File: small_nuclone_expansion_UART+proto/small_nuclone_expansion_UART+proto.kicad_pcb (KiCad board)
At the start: 2 copper layers, 50 x 50 mm, 87 parts, among them J1 USB-C_PD_USB, J2 Conn_01x16, J3 nuclone_small_left, J4 nuclone_small_right, J5 127, J6 127, J7 127, J8 127, U1 TPESD0504C6, U2 CH340B

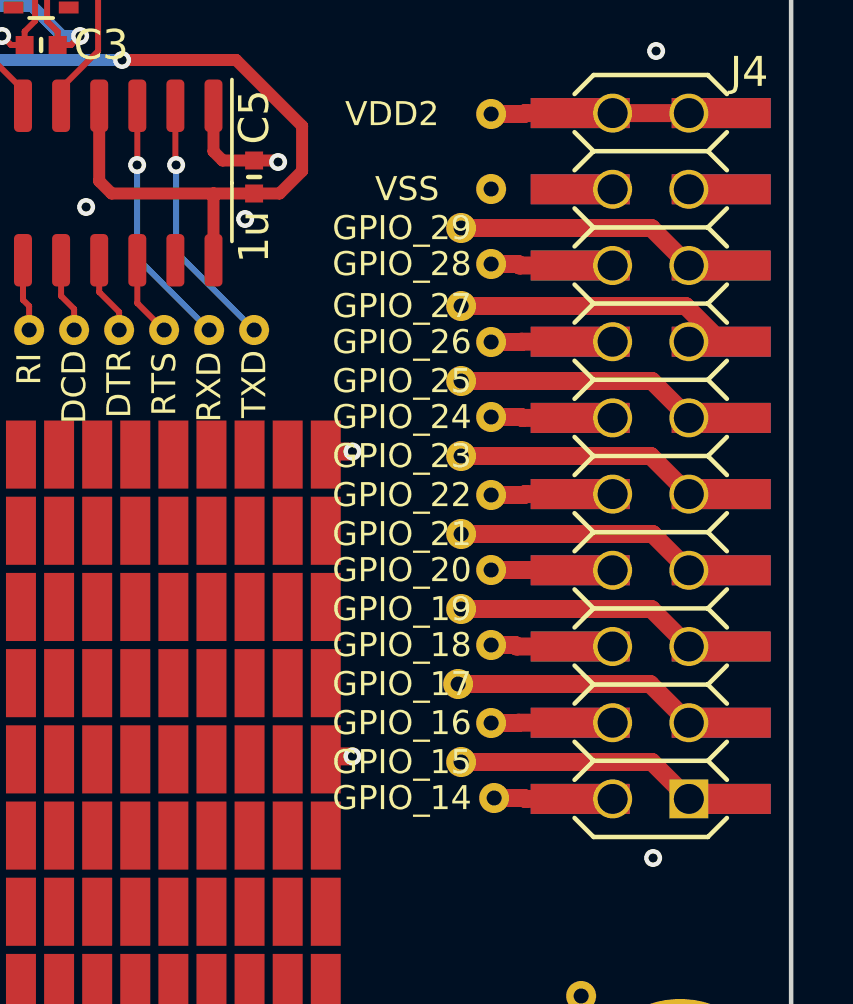
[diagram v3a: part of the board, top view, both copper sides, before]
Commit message: changed pin labels
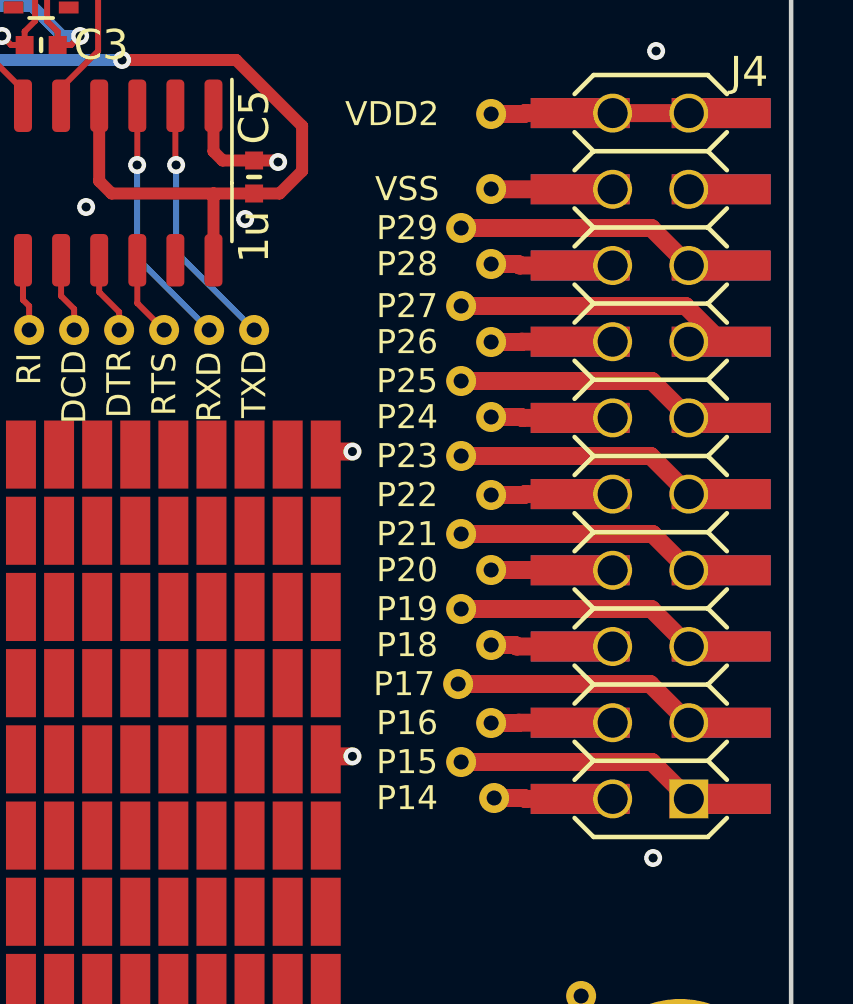
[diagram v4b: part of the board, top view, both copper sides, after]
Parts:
- TP20: value GPIO_29 -> P29
- TP21: value GPIO_28 -> P28
- TP22: value GPIO_27 -> P27
- TP23: value GPIO_26 -> P26
- TP24: value GPIO_25 -> P25
- TP25: value GPIO_24 -> P24
- TP26: value GPIO_23 -> P23
- TP27: value GPIO_22 -> P22
- TP28: value GPIO_21 -> P21
- TP29: value GPIO_20 -> P20
- TP30: value GPIO_19 -> P19
- TP31: value GPIO_18 -> P18
- TP32: value GPIO_17 -> P17
- TP33: value GPIO_16 -> P16
- TP34: value GPIO_15 -> P15
- TP35: value GPIO_14 -> P14
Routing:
- net /VSS: track 20.2 -> 23.2 mm
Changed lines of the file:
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@@
     (thickness 1.6)
     (drawings 19)
-    (tracks 293)
+    (tracks 295)
     (zones 0)
     (modules 87)
@@
   )
   (setup
-    (last_trace_width 0.2)
+    (last_trace_width 0.6)
     (user_trace_width 0.15)
     (user_trace_width 0.2)
@@
       (effects (font (size 1 1) (thickness 0.15)))
     )
-    (fp_text value GPIO_14 (at -3.072 0) (layer F.SilkS)
+    (fp_text value P14 (at -2.9 0) (layer F.SilkS)
       (effects (font (size 0.8 0.8) (thickness 0.12)))
     )
@@
       (effects (font (size 1 1) (thickness 0.15)))
     )
-    (fp_text value GPIO_15 (at -1.972 0) (layer F.SilkS)
+    (fp_text value P15 (at -1.8 0) (layer F.SilkS)
       (effects (font (size 0.8 0.8) (thickness 0.12)))
     )
@@
       (effects (font (size 1 1) (thickness 0.15)))
     )
-    (fp_text value GPIO_16 (at -2.972 0) (layer F.SilkS)
+    (fp_text value P16 (at -2.8 0) (layer F.SilkS)
       (effects (font (size 0.8 0.8) (thickness 0.12)))
     )
@@
       (effects (font (size 1 1) (thickness 0.15)))
     )
-    (fp_text value GPIO_17 (at -1.872 0) (layer F.SilkS)
+    (fp_text value P17 (at -1.8 0) (layer F.SilkS)
       (effects (font (size 0.8 0.8) (thickness 0.12)))
     )
@@
       (effects (font (size 1 1) (thickness 0.15)))
     )
-    (fp_text value GPIO_18 (at -2.972 0) (layer F.SilkS)
+    (fp_text value P18 (at -2.8 0) (layer F.SilkS)
       (effects (font (size 0.8 0.8) (thickness 0.12)))
     )
@@
       (effects (font (size 1 1) (thickness 0.15)))
     )
-    (fp_text value GPIO_19 (at -1.972 0) (layer F.SilkS)
+    (fp_text value P19 (at -1.8 0) (layer F.SilkS)
       (effects (font (size 0.8 0.8) (thickness 0.12)))
     )
@@
       (effects (font (size 1 1) (thickness 0.15)))
     )
-    (fp_text value GPIO_20 (at -2.972 0) (layer F.SilkS)
+    (fp_text value P20 (at -2.8 0) (layer F.SilkS)
       (effects (font (size 0.8 0.8) (thickness 0.12)))
     )
@@
       (effects (font (size 1 1) (thickness 0.15)))
     )
-    (fp_text value GPIO_21 (at -1.972 0) (layer F.SilkS)
+    (fp_text value P21 (at -1.8 0) (layer F.SilkS)
       (effects (font (size 0.8 0.8) (thickness 0.12)))
     )
@@
       (effects (font (size 1 1) (thickness 0.15)))
     )
-    (fp_text value GPIO_22 (at -2.972 0) (layer F.SilkS)
+    (fp_text value P22 (at -2.8 0) (layer F.SilkS)
       (effects (font (size 0.8 0.8) (thickness 0.12)))
     )
@@
       (effects (font (size 1 1) (thickness 0.15)))
     )
-    (fp_text value GPIO_23 (at -1.972 0) (layer F.SilkS)
+    (fp_text value P23 (at -1.8 0) (layer F.SilkS)
       (effects (font (size 0.8 0.8) (thickness 0.12)))
     )
@@
       (effects (font (size 1 1) (thickness 0.15)))
     )
-    (fp_text value GPIO_24 (at -2.972 0) (layer F.SilkS)
+    (fp_text value P24 (at -2.8 0) (layer F.SilkS)
       (effects (font (size 0.8 0.8) (thickness 0.12)))
     )
@@
       (effects (font (size 1 1) (thickness 0.15)))
     )
-    (fp_text value GPIO_25 (at -1.972 0) (layer F.SilkS)
+    (fp_text value P25 (at -1.8 0) (layer F.SilkS)
       (effects (font (size 0.8 0.8) (thickness 0.12)))
     )
@@
       (effects (font (size 1 1) (thickness 0.15)))
     )
-    (fp_text value GPIO_26 (at -2.972 0) (layer F.SilkS)
+    (fp_text value P26 (at -2.8 0) (layer F.SilkS)
       (effects (font (size 0.8 0.8) (thickness 0.12)))
     )
@@
       (effects (font (size 1 1) (thickness 0.15)))
     )
-    (fp_text value GPIO_27 (at -1.972 0) (layer F.SilkS)
+    (fp_text value P27 (at -1.8 0) (layer F.SilkS)
       (effects (font (size 0.8 0.8) (thickness 0.12)))
     )
@@
       (effects (font (size 1 1) (thickness 0.15)))
     )
-    (fp_text value GPIO_28 (at -2.972 0) (layer F.SilkS)
+    (fp_text value P28 (at -2.8 0) (layer F.SilkS)
       (effects (font (size 0.8 0.8) (thickness 0.12)))
     )
@@
       (effects (font (size 1 1) (thickness 0.15)))
     )
-    (fp_text value GPIO_29 (at -1.972 0) (layer F.SilkS)
+    (fp_text value P29 (at -1.8 0) (layer F.SilkS)
       (effects (font (size 0.8 0.8) (thickness 0.12)))
     )
@@
   (segment (start 75.438 93.472) (end 74.549 93.472) (width 0.6) (layer F.Cu) (net 2))
   (via (at 74.549 93.472) (size 0.6) (drill 0.3) (layers F.Cu B.Cu) (net 2))
+  (segment (start 100.01 77.11) (end 100 77.1) (width 0.6) (layer F.Cu) (net 2))
+  (segment (start 102.97 77.11) (end 100.01 77.11) (width 0.6) (layer F.Cu) (net 2))
   (segment (start 100 79.6) (end 100.9 79.6) (width 0.6) (layer F.Cu) (net 3))
   (segment (start 100.95 79.65) (end 102.97 79.65) (width 0.6) (layer F.Cu) (net 3))

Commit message: conversion to kicad6
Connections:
- J1 pad A8: Net-(J1-PadA8) -> unconnected-(J1-PadA8)
- J1 pad B8: Net-(J1-PadB8) -> unconnected-(J1-PadB8)
- U1 pad 3: Net-(U1-Pad3) -> unconnected-(U1-Pad3)
- U1 pad 4: Net-(U1-Pad4) -> unconnected-(U1-Pad4)
- U2 pad 15: Net-(U2-Pad15) -> unconnected-(U2-Pad15)
- U2 pad 7: Net-(U2-Pad7) -> unconnected-(U2-Pad7)
- U2 pad 8: Net-(U2-Pad8) -> unconnected-(U2-Pad8)
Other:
- net class Default removed
- net class Power removed
- net class Signal removed

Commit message: updated pads
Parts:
- N2: value V20220215 -> V20220513
- TP1, TP10, TP11, TP12, TP13, TP14, TP15, TP16, TP17, TP18, TP19, TP2, TP20, TP21, TP22, TP23, TP24, TP25, TP26, TP27, TP28, TP29, TP3, TP30, TP31, TP32, TP33, TP34, TP35, TP36, TP37, TP38, TP39, TP4, TP40, TP41, TP42, TP43, TP5, TP6, TP60, TP61, TP7, TP8, TP9: footprint SquantorTestPoints:TestPoint_hole_H05R10_small_text -> SquantorTestPoints:TestPoint_hole_H05R10_2side
- moved TP36 0.50 mm to (91.8, 81.4)
- moved TP37 0.50 mm to (90.3, 81.4)
- moved TP38 0.50 mm to (88.8, 81.4)
- moved TP39 0.50 mm to (87.3, 81.4)
- moved TP40 0.50 mm to (85.8, 81.4)
- moved TP41 0.50 mm to (84.3, 81.4)
- moved TP42 0.50 mm to (82.8, 81.4)
- moved TP43 0.50 mm to (81.3, 81.4)
- moved TP32 0.41 mm to (99.3, 93.6)
- moved TP22 0.33 mm to (99.3, 80.9)
- moved TP28 0.32 mm to (99.3, 88.5)
- moved TP24 0.32 mm to (99.3, 83.4)
- moved TP34 0.32 mm to (99.3, 96.1)
- moved TP20 0.32 mm to (99.3, 78.4)
- moved TP30 0.32 mm to (99.3, 91.1)
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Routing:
- net /VSS: track 23.2 -> 18.2 mm
- net /VUSB: track 16.7 -> 18.6 mm
- net /GPIO_27: track 9.16 -> 7.81 mm
- net /GPIO_06: track 9.07 -> 7.74 mm
- net /TXD: track 8.56 -> 8.04 mm
- net /DCD: track 2.51 -> 1.98 mm
- net /RXD: track 8.47 -> 7.95 mm
- net /DTR: track 2.60 -> 2.08 mm
- net /RTS: track 2.70 -> 2.17 mm
